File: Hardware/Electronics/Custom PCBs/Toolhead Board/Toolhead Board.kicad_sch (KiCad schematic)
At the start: 14 parts, among them U1 LF15_TO220, U2 LF15_TO220

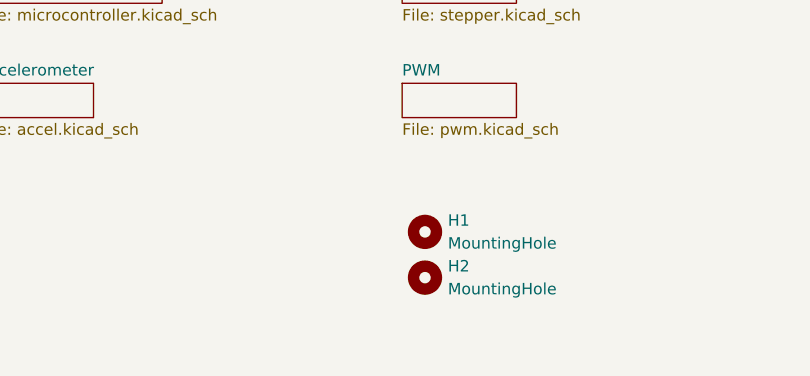
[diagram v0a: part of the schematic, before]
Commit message: Update toolhead board layout
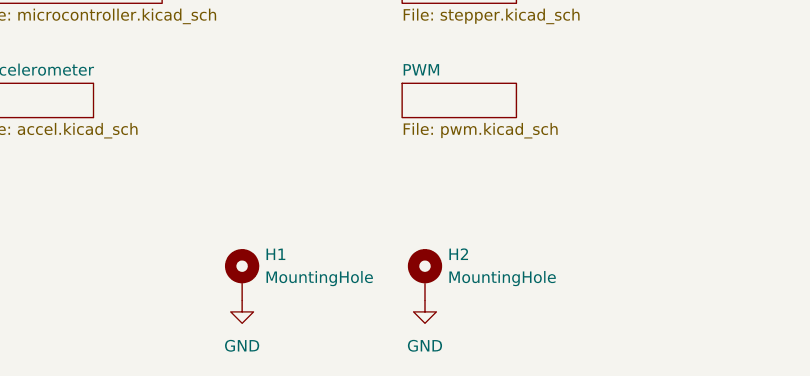
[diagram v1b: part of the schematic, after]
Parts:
- H1: symbol Mechanical:MountingHole -> Mechanical:MountingHole_Pad; now in the parts list
- H2: footprint MountingHole:MountingHole_3.2mm_M3_DIN965_Pad -> MountingHole:MountingHole_2.2mm_M2_Pad; symbol Mechanical:MountingHole -> Mechanical:MountingHole_Pad; now in the parts list
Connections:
- net GND: now also H1.1, H2.1
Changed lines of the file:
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@@
 	)
 	(symbol
-		(lib_id "Mechanical:MountingHole")
-		(at 149.86 73.66 0)
-		(unit 1)
-		(exclude_from_sim yes)
-		(in_bom no)
+		(lib_id "Mechanical:MountingHole_Pad")
+		(at 129.54 78.74 0)
+		(unit 1)
+		(exclude_from_sim no)
+		(in_bom yes)
 		(on_board yes)
 		(dnp no)
 		(fields_autoplaced yes)
 		(property "Reference" "H1"
-			(at 152.4 72.3899 0)
+			(at 132.08 76.1999 0)
 			(effects
 				(font
@@
 		)
 		(property "Value" "MountingHole"
-			(at 152.4 74.9299 0)
+			(at 132.08 78.7399 0)
 			(effects
 				(font
@@
 		)
 		(property "Footprint" "MountingHole:MountingHole_3.2mm_M3_DIN965_Pad"
-			(at 149.86 73.66 0)
+			(at 129.54 78.74 0)
 			(effects
 				(font
@@
 		)
 		(property "Datasheet" "~"
-			(at 149.86 73.66 0)
-			(effects
-				(font
-					(size 1.27 1.27)
-				)
-				(hide yes)
-			)
-		)
-		(property "Description" "Mounting Hole without connection"
-			(at 149.86 73.66 0)
-			(effects
-				(font
-					(size 1.27 1.27)
-				)
-				(hide yes)
-			)
+			(at 129.54 78.74 0)
+			(effects
+				(font
+					(size 1.27 1.27)
+				)
+				(hide yes)
+			)
+		)
+		(property "Description" "Mounting Hole with connection"
+			(at 129.54 78.74 0)
+			(effects
+				(font
+					(size 1.27 1.27)
+				)
+				(hide yes)
+			)
+		)
+		(pin "1"
 		)
 		(instances
@@
 				(path "/a1747683-152e-4245-ab61-2d33ce6021ef"
 					(reference "H1")
+					(unit 1)
+				)
+			)
+		)
+	)
+	(symbol
+		(lib_name "GND_1")
+		(lib_id "power:GND")
+		(at 129.54 81.28 0)
+		(unit 1)
+		(exclude_from_sim no)
+		(in_bom yes)
+		(on_board yes)
+		(dnp no)
+		(fields_autoplaced yes)
+		(property "Reference" "#PWR045"
+			(at 129.54 87.63 0)
+			(effects
+				(font
+					(size 1.27 1.27)
+				)
+				(hide yes)
+			)
+		)
+		(property "Value" "GND"
+			(at 129.54 86.36 0)
+			(effects
+				(font
+					(size 1.27 1.27)
+				)
+			)
+		)
+		(property "Footprint" ""
+			(at 129.54 81.28 0)
+			(effects
+				(font
+					(size 1.27 1.27)
+				)
+				(hide yes)
+			)
+		)
+		(property "Datasheet" ""
+			(at 129.54 81.28 0)
+			(effects
+				(font
+					(size 1.27 1.27)
+				)
+				(hide yes)
+			)
+		)
+		(property "Description" "Power symbol creates a global label with name \"GND\" , ground"
+			(at 129.54 81.28 0)
+			(effects
+				(font
+					(size 1.27 1.27)
+				)
+				(hide yes)
+			)
+		)
+		(pin "1"
+		)
+		(instances
+			(project "Toolhead Board"
+				(path "/a1747683-152e-4245-ab61-2d33ce6021ef"
+					(reference "#PWR045")
 					(unit 1)
 				)
@@
 	)
 	(symbol
-		(lib_id "Mechanical:MountingHole")
+		(lib_id "Mechanical:MountingHole_Pad")
 		(at 149.86 78.74 0)
 		(unit 1)
-		(exclude_from_sim yes)
-		(in_bom no)
+		(exclude_from_sim no)
+		(in_bom yes)
 		(on_board yes)
 		(dnp no)
 		(fields_autoplaced yes)
 		(property "Reference" "H2"
-			(at 152.4 77.4699 0)
+			(at 152.4 76.1999 0)
 			(effects
 				(font
@@
 		)
 		(property "Value" "MountingHole"
-			(at 152.4 80.0099 0)
-			(effects
-				(font
-					(size 1.27 1.27)
-				)
-				(justify left)
-			)
-		)
-		(property "Footprint" "MountingHole:MountingHole_3.2mm_M3_DIN965_Pad"
+			(at 152.4 78.7399 0)
+			(effects
+				(font
+					(size 1.27 1.27)
+				)
+				(justify left)
+			)
+		)
+		(property "Footprint" "MountingHole:MountingHole_2.2mm_M2_Pad"
 			(at 149.86 78.74 0)
 			(effects
@@
 			)
 		)
-		(property "Description" "Mounting Hole without connection"
+		(property "Description" "Mounting Hole with connection"
 			(at 149.86 78.74 0)
 			(effects
@@
 				(hide yes)
 			)
+		)
+		(pin "1"
 		)
 		(instances
@@
 					(unit 1)
 				)
+			)
+		)
+	)
+	(symbol
+		(lib_name "GND_1")
+		(lib_id "power:GND")
+		(at 149.86 81.28 0)
+		(unit 1)
+		(exclude_from_sim no)
+		(in_bom yes)
+		(on_board yes)
+		(dnp no)
+		(fields_autoplaced yes)
+		(property "Reference" "#PWR039"
+			(at 149.86 87.63 0)
+			(effects
+				(font
+					(size 1.27 1.27)
+				)
+				(hide yes)
+			)
+		)
+		(property "Value" "GND"
+			(at 149.86 86.36 0)
+			(effects
+				(font
+					(size 1.27 1.27)
+				)
+			)
+		)
+		(property "Footprint" ""
+			(at 149.86 81.28 0)
+			(effects
+				(font
+					(size 1.27 1.27)
+				)
+				(hide yes)
+			)
+		)
+		(property "Datasheet" ""
+			(at 149.86 81.28 0)
+			(effects
+				(font
+					(size 1.27 1.27)
+				)
+				(hide yes)
+			)
+		)
+		(property "Description" "Power symbol creates a global label with name \"GND\" , ground"
+			(at 149.86 81.28 0)
+			(effects
+				(font
+					(size 1.27 1.27)
+				)
+				(hide yes)
+			)
+		)
+		(pin "1"
+		)
+		(instances
+			(project "Toolhead Board"
+				(path "/a1747683-152e-4245-ab61-2d33ce6021ef"
+					(reference "#PWR039")
+					(unit 1)
+				)

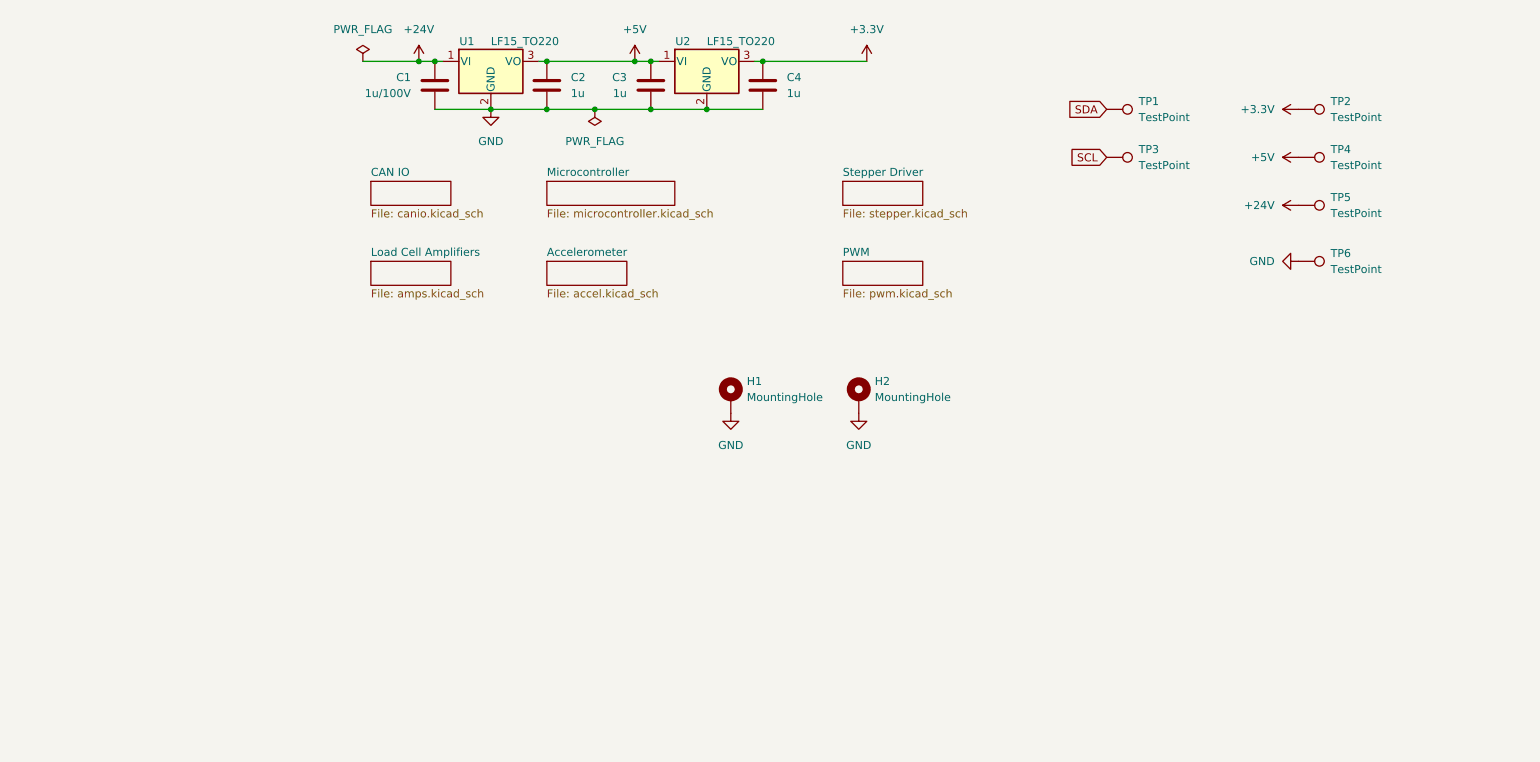
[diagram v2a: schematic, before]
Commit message: Update toolhead schematic+layout and add tolerances to base
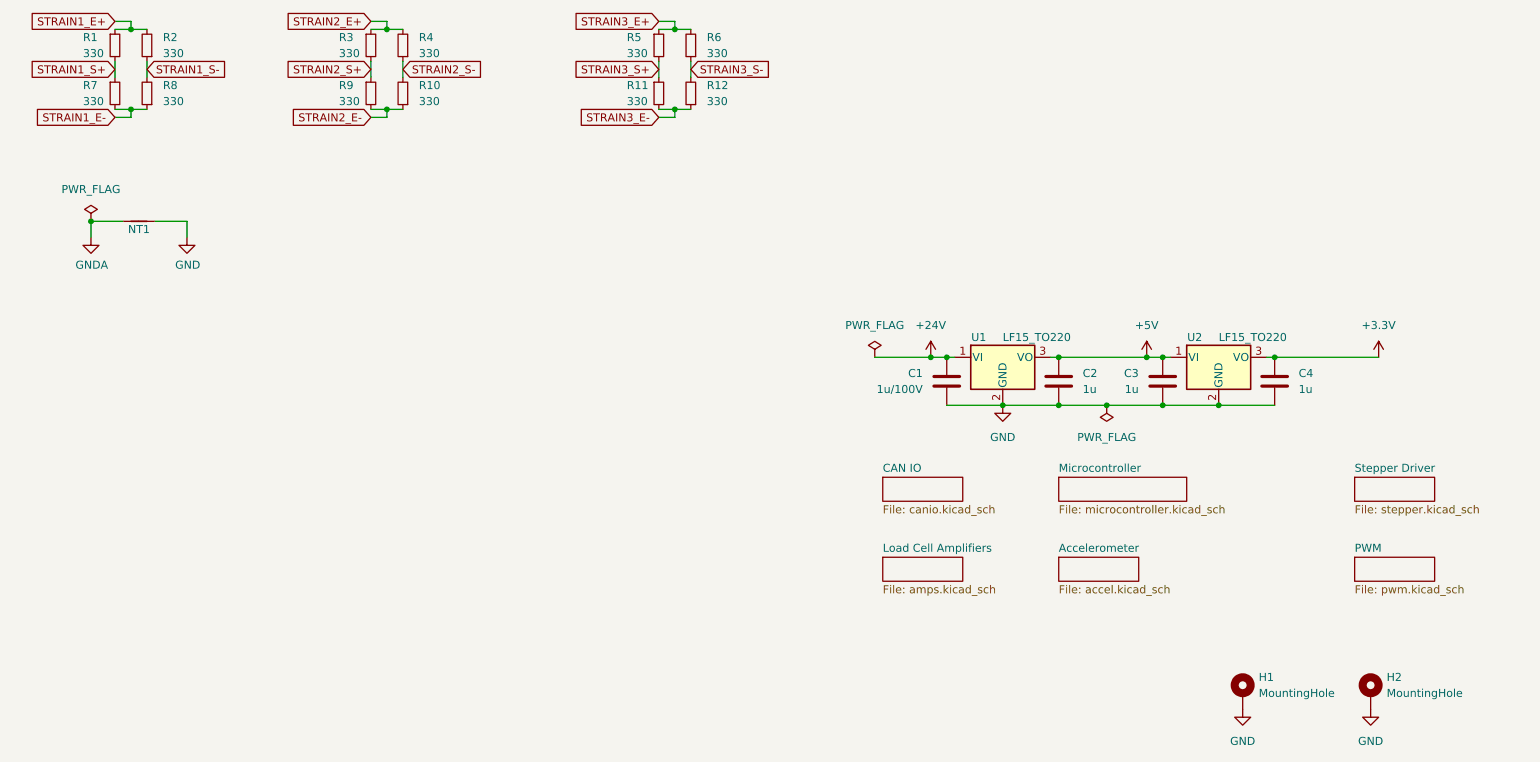
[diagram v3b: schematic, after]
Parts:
- removed TP1, TP2, TP3, TP4, TP5: TestPoint, TestPoint:TestPoint_Pad_D1.5mm, symbol Connector:TestPoint
- removed TP6: TestPoint, TestPoint:TestPoint_Pad_1.5x1.5mm, symbol Connector:TestPoint
- added NT1: NetTie_2, NetTie:NetTie-2_SMD_Pad0.5mm, symbol Device:NetTie_2
- added R1, R10, R11, R12, R2, R3, R4, R5, R6, R7, R8, R9: 330, Resistor_SMD:R_2512_6332Metric, symbol Device:R_Small
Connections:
- net GND: now also NT1.2
- new net GNDA: NT1.1
- new net STRAIN1_E+: R1.1, R2.2
- new net STRAIN1_E-: R7.2, R8.1
- new net STRAIN1_S+: R1.2, R7.1
- new net STRAIN1_S-: R2.1, R8.2
- new net STRAIN2_E+: R3.1, R4.2
- new net STRAIN2_E-: R10.1, R9.2
- new net STRAIN2_S+: R3.2, R9.1
- new net STRAIN2_S-: R10.2, R4.1
- new net STRAIN3_E+: R5.1, R6.2
- new net STRAIN3_E-: R11.2, R12.1
- new net STRAIN3_S+: R11.1, R5.2
- new net STRAIN3_S-: R12.2, R6.1
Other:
- moved on the sheet: C1, C2, C3, C4, H1, H2, U1, U2

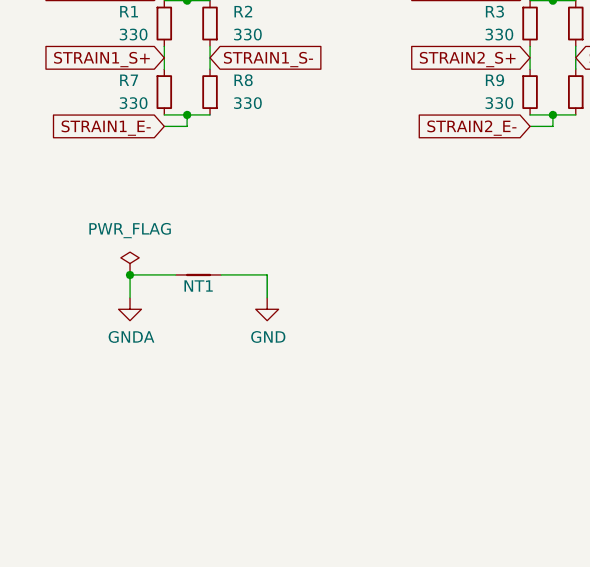
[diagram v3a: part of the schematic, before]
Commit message: Update toolhead PCB layout
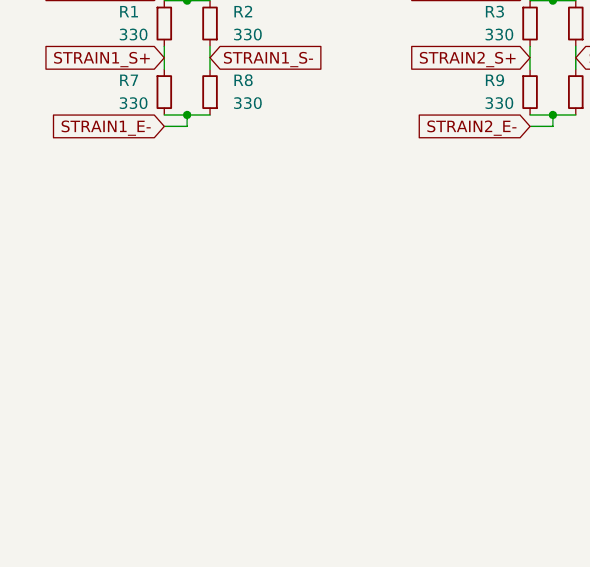
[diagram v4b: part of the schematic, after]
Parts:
- removed NT1: NetTie_2, NetTie:NetTie-2_SMD_Pad0.5mm, symbol Device:NetTie_2
